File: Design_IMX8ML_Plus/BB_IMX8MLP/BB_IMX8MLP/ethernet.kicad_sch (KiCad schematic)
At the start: 3 parts, among them J5 RJ45_Amphenol_RJMG1BD3B8K1ANR, J6 RJ45_Amphenol_RJMG1BD3B8K1ANR, U1 KSZ9131RNXI

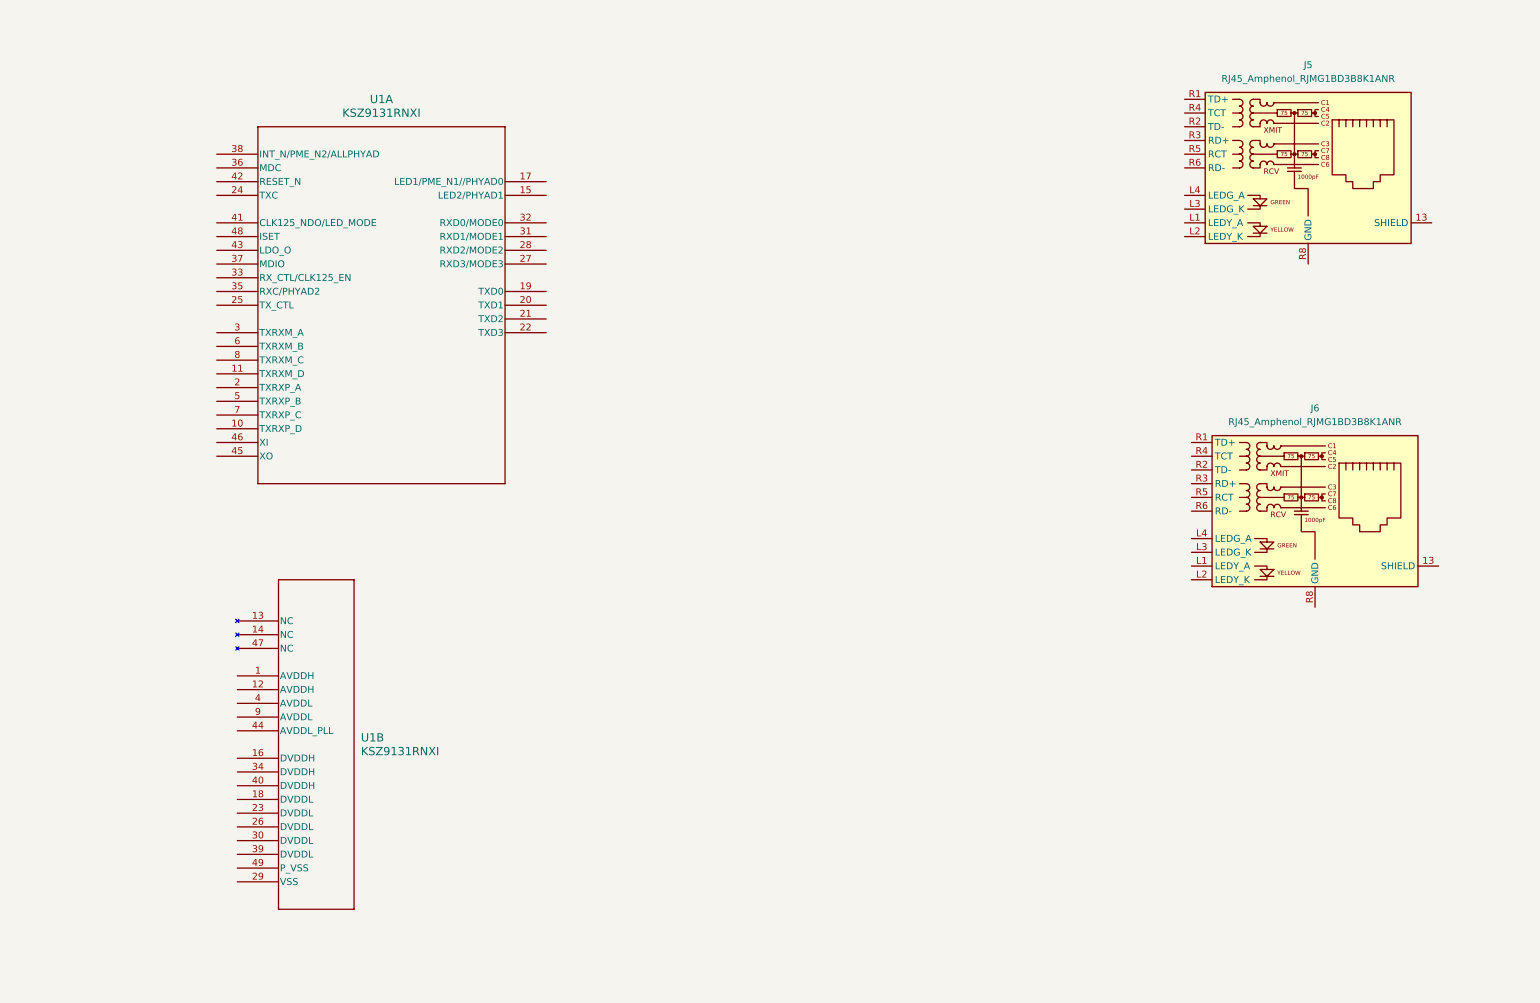
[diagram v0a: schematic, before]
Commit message: Add SPB228 WIFI/BLE module
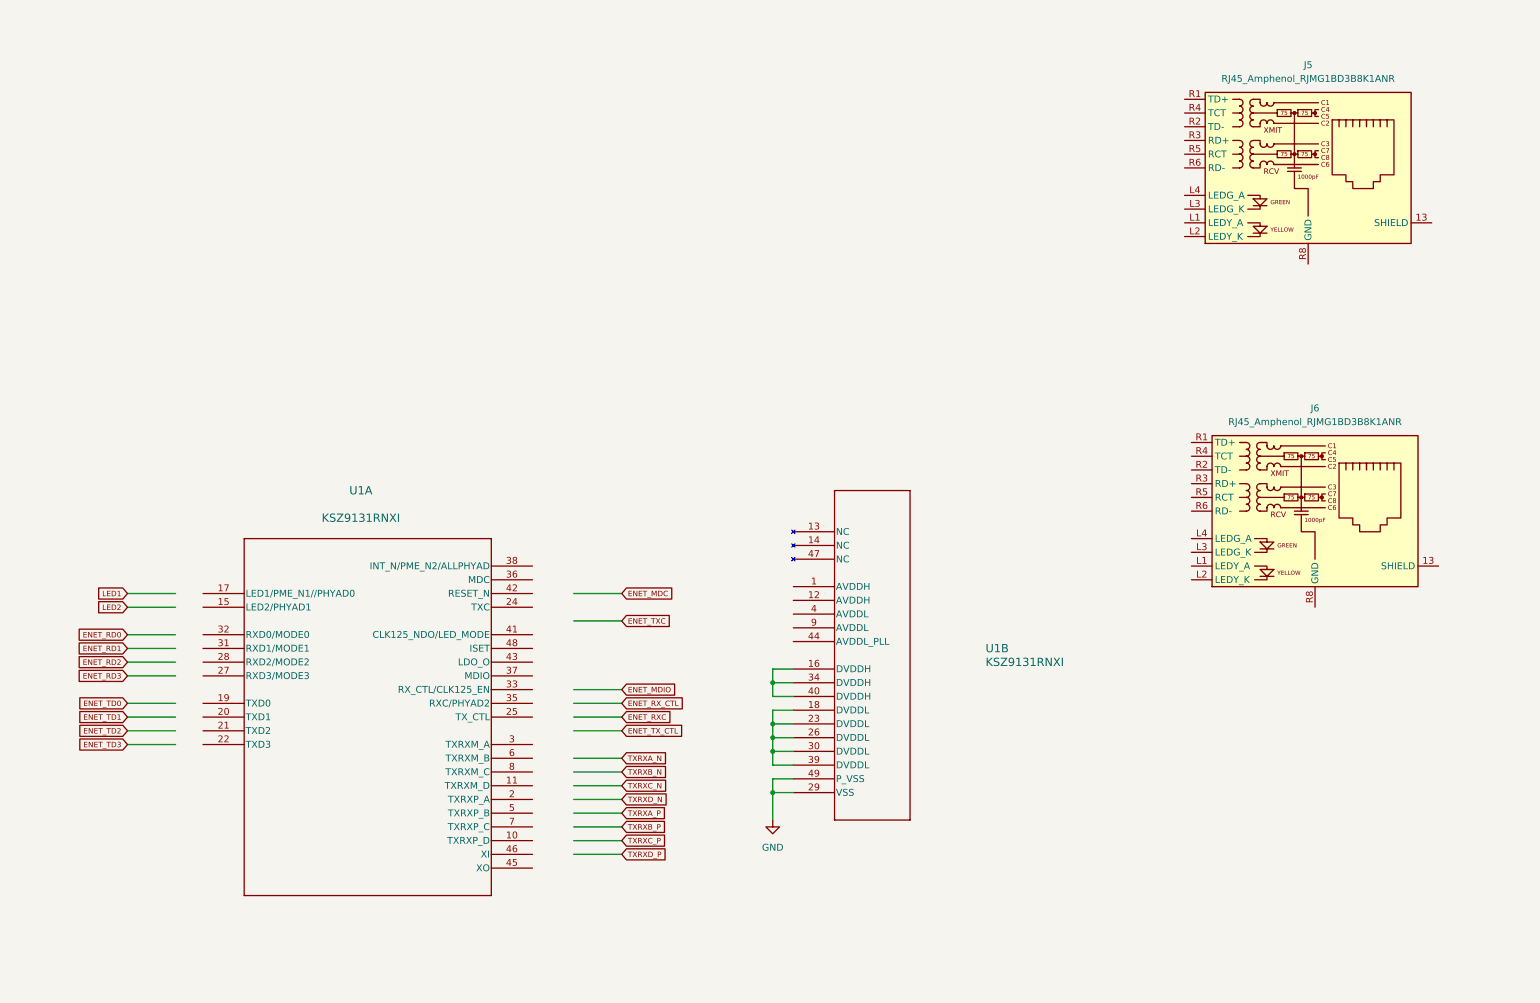
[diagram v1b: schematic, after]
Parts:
- U1: footprint QFN48_7X7_MCH -> Package_DFN_QFN:QFN-48-1EP_7x7mm_P0.5mm_EP5.6x5.6mm
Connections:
- net at U1.16 (DVDDH): now also U1.34 (DVDDH), U1.40 (DVDDH)
- net at U1.18 (DVDDL): now also U1.23 (DVDDL), U1.26 (DVDDL), U1.30 (DVDDL), U1.39 (DVDDL)
- net GND: now reaches U1.29 (VSS)
- net GND: now also U1.49 (P_VSS)

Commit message: improving the usb conector
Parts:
- added C65, C66: 12Pf, Capacitor_SMD:C_0402_1005Metric, symbol Device:C_Small
- added Y2: 25MHz, Crystal:Crystal_SMD_0603-4Pin_6.0x3.5mm, symbol Device:Crystal_GND24_Small
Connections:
- net ENET_MDC: now also U1.36 (MDC)
- net ENET_TXC: now also U1.24 (TXC)
- net GND: now also C65.2, C66.2, Y2.2, Y2.4
- net CTRL_RESET: now reaches U1.42 (RESET_N)
- net at U1.45 (XO): now also C66.1, Y2.3
- net at U1.46 (XI): now also C65.1, Y2.1
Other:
- moved on the sheet: U1B

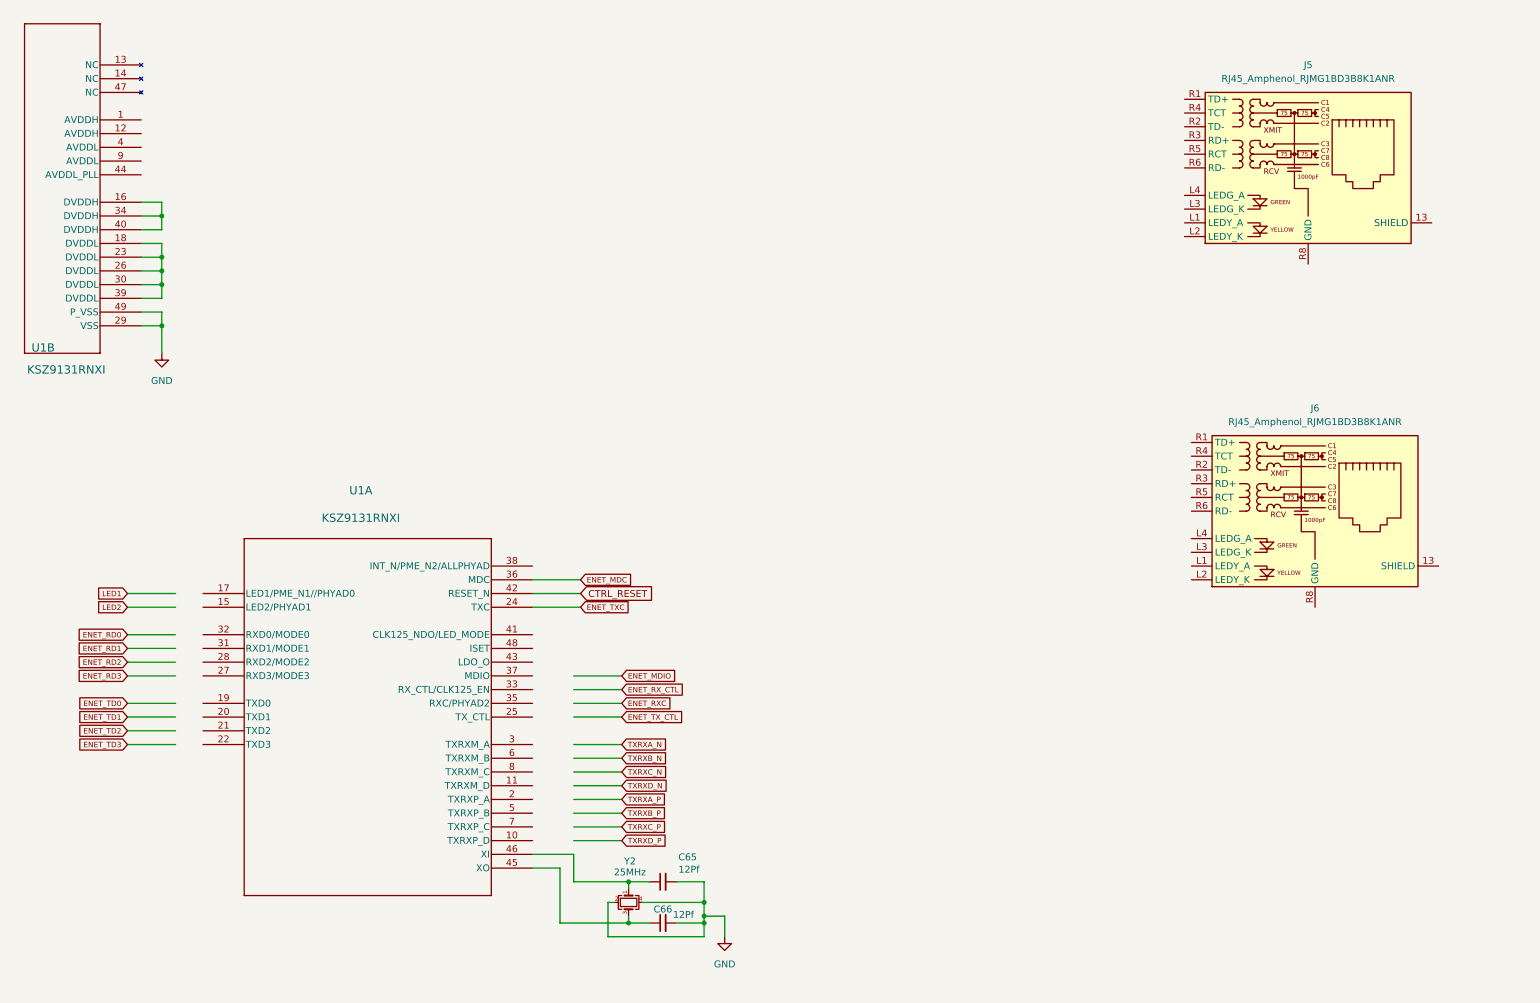
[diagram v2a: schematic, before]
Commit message: improving Ethernet, USB and Camera inteface
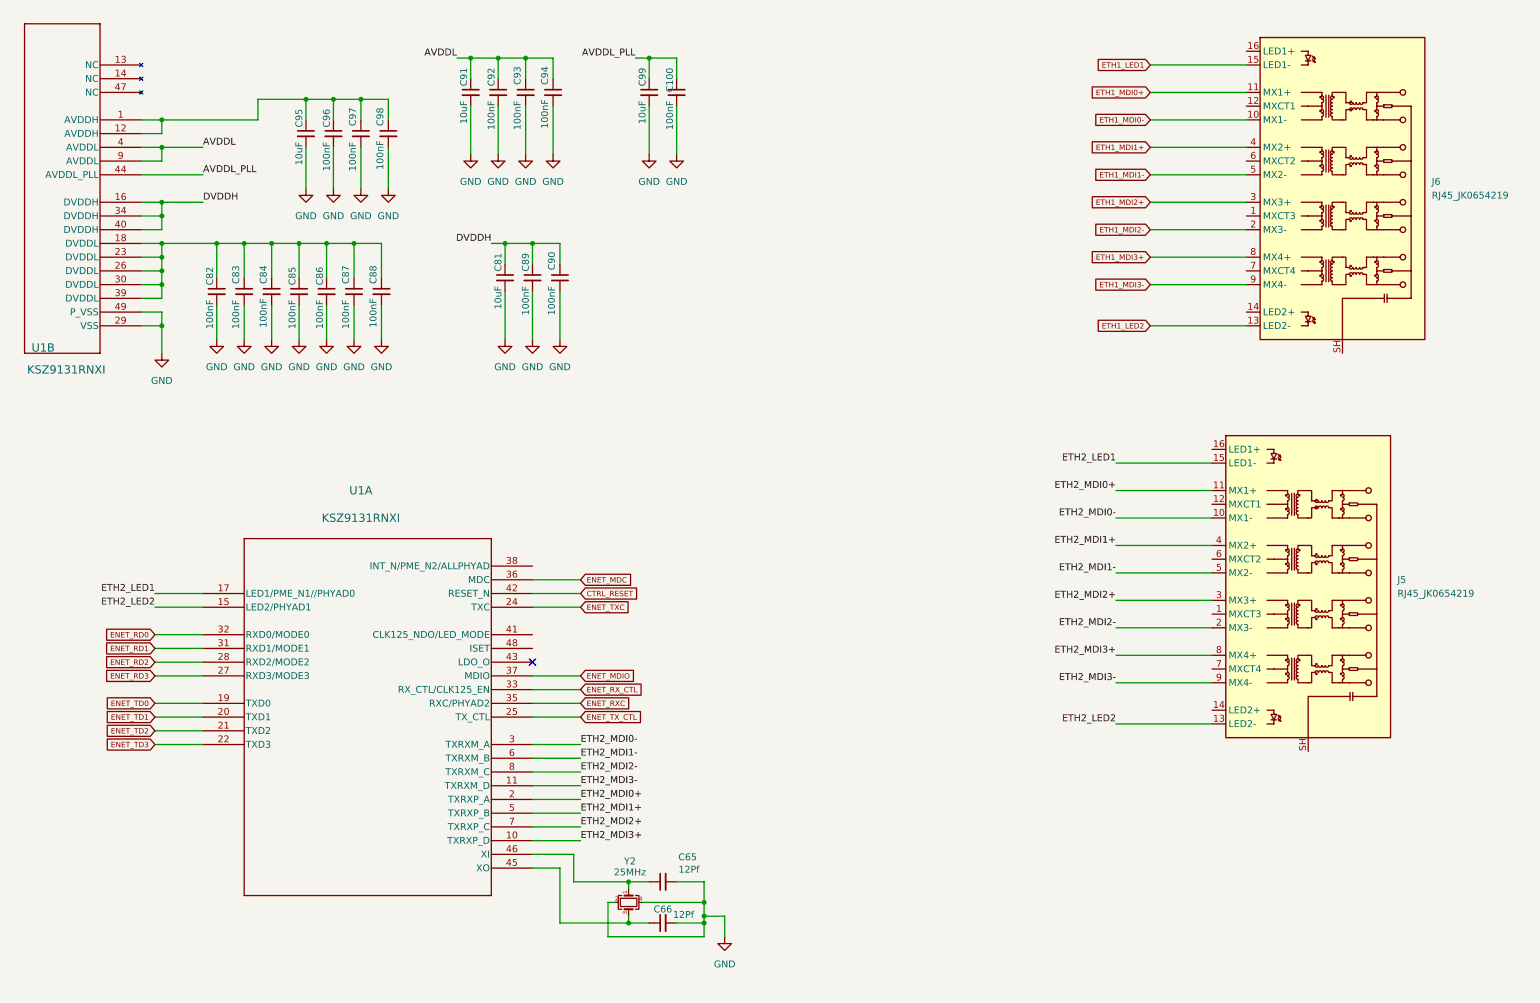
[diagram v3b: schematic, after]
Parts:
- removed J5, J6: RJ45_Amphenol_RJMG1BD3B8K1ANR, Connector_RJ:RJ45_Amphenol_RJMG1BD3B8K1ANR, symbol Connector:RJ45_Amphenol_RJMG1BD3B8K1ANR
- added C100, C82, C83, C84, C85, C86, C87, C88, C89, C90, C92, C93, C94, C96, C97, C98: 100nF, Capacitor_SMD:C_0402_1005Metric, symbol Device:C_Small
- added C81, C91, C95, C99: 10uF, Capacitor_SMD:C_0402_1005Metric, symbol Device:C_Small
- added J5, J6: RJ45_JK0654219, Connector_RJ:RJ45_Pulse_JK0654219NL_Horizontal, symbol Connector:RJ45_JK0654219
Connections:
- net ENET_MDIO: now also U1.37 (MDIO)
- net ENET_RD0: now also U1.32 (RXD0/MODE0)
- net ENET_RD1: now also U1.31 (RXD1/MODE1)
- net ENET_RD2: now also U1.28 (RXD2/MODE2)
- net ENET_RD3: now also U1.27 (RXD3/MODE3)
- net ENET_RXC: now also U1.35 (RXC/PHYAD2)
- net ENET_RX_CTL: now also U1.33 (RX_CTL/CLK125_EN)
- net ENET_TD0: now also U1.19 (TXD0)
- net ENET_TD1: now also U1.20 (TXD1)
- net ENET_TD2: now also U1.21 (TXD2)
- net ENET_TD3: now also U1.22 (TXD3)
- net ENET_TX_CTL: now also U1.25 (TX_CTL)
- net GND: now also C100.2, C81.2, C82.2, C83.2, C84.2, C85.2, C86.2, C87.2, C88.2, C89.2, C90.2, C91.2, C92.2, C93.2, C94.2, C95.2, C96.2, C97.2, C98.2, C99.2
- net at U1.1 (AVDDH): now also U1.12 (AVDDH), C95.1, C96.1, C97.1, C98.1
- net DVDDH: now reaches U1.16 (DVDDH), U1.34 (DVDDH), U1.40 (DVDDH)
- net DVDDH: now also C81.1, C89.1, C90.1
- net at U1.18 (DVDDL), U1.23 (DVDDL), U1.26 (DVDDL)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: now also C82.1, C83.1, C84.1, C85.1, C86.1, C87.1, C88.1
- net AVDDL: now reaches U1.4 (AVDDL)
- net AVDDL: now also U1.9 (AVDDL), C91.1, C92.1, C93.1, C94.1
- net AVDDL_PLL: now reaches U1.44 (AVDDL_PLL)
- net AVDDL_PLL: now also C100.1, C99.1
- net ETH2_MDI3+: now reaches U1.10 (TXRXP_D)
- net ETH2_MDI3+: now also J5.8 (MX4+)
- net ETH2_MDI3-: now reaches U1.11 (TXRXM_D)
- net ETH2_MDI3-: now also J5.9 (MX4-)
- net ETH2_LED2: now reaches U1.15 (LED2/PHYAD1)
- net ETH2_LED2: now also J5.13 (LED2-)
- net ETH2_LED1: now reaches U1.17 (LED1/PME_N1//PHYAD0)
- net ETH2_LED1: now also J5.15 (LED1-)
- net ETH2_MDI0+: now reaches U1.2 (TXRXP_A)
- net ETH2_MDI0+: now also J5.11 (MX1+)
- net ETH2_MDI0-: now reaches U1.3 (TXRXM_A)
- net ETH2_MDI0-: now also J5.10 (MX1-)
- net ETH2_MDI1+: now reaches U1.5 (TXRXP_B)
- net ETH2_MDI1+: now also J5.4 (MX2+)
- net ETH2_MDI1-: now reaches U1.6 (TXRXM_B)
- net ETH2_MDI1-: now also J5.5 (MX2-)
- net ETH2_MDI2+: now reaches U1.7 (TXRXP_C)
- net ETH2_MDI2+: now also J5.3 (MX3+)
- net ETH2_MDI2-: now reaches U1.8 (TXRXM_C)
- net ETH2_MDI2-: now also J5.2 (MX3-)
- new net ETH1_LED1: J6.15 (LED1-)
- new net ETH1_LED2: J6.13 (LED2-)
- new net ETH1_MDI0+: J6.11 (MX1+)
- new net ETH1_MDI0-: J6.10 (MX1-)
- new net ETH1_MDI1+: J6.4 (MX2+)
- new net ETH1_MDI1-: J6.5 (MX2-)
- new net ETH1_MDI2+: J6.3 (MX3+)
- new net ETH1_MDI2-: J6.2 (MX3-)
- new net ETH1_MDI3+: J6.8 (MX4+)
- new net ETH1_MDI3-: J6.9 (MX4-)
- no-connect marks 0 -> 1
